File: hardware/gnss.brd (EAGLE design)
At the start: 33.5 x 34.6 mm, 39 parts, among them J1 MICRO_USB_B_HIROSE_ZX62-B-5PA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, SW1 TVAF06-A020B-R, U2 NJM12888F, X1 FA-238

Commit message: communication基盤一部改良、GNSS基盤
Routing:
- net GND: track 112.9 -> 180.1 mm, vias 71 -> 70
- net N$1: track 0.00 -> 35.7 mm, vias 0 -> 3
- net N$3: track 0.00 -> 22.1 mm, vias 0 -> 2
- net VDD: track 73.0 -> 91.8 mm, vias 6 -> 7
- net N$2: track 0.00 -> 3.50 mm

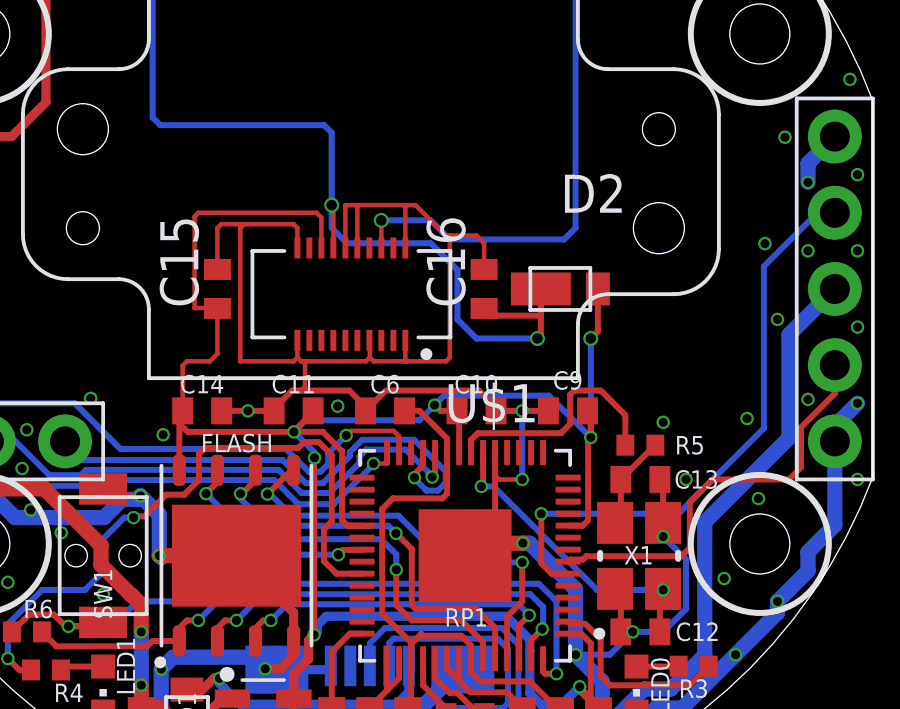
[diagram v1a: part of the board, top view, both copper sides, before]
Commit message: 変更点: communication_LoRaをUART接続に変換 gnss_GPSのRTX接続およびRESETの追加
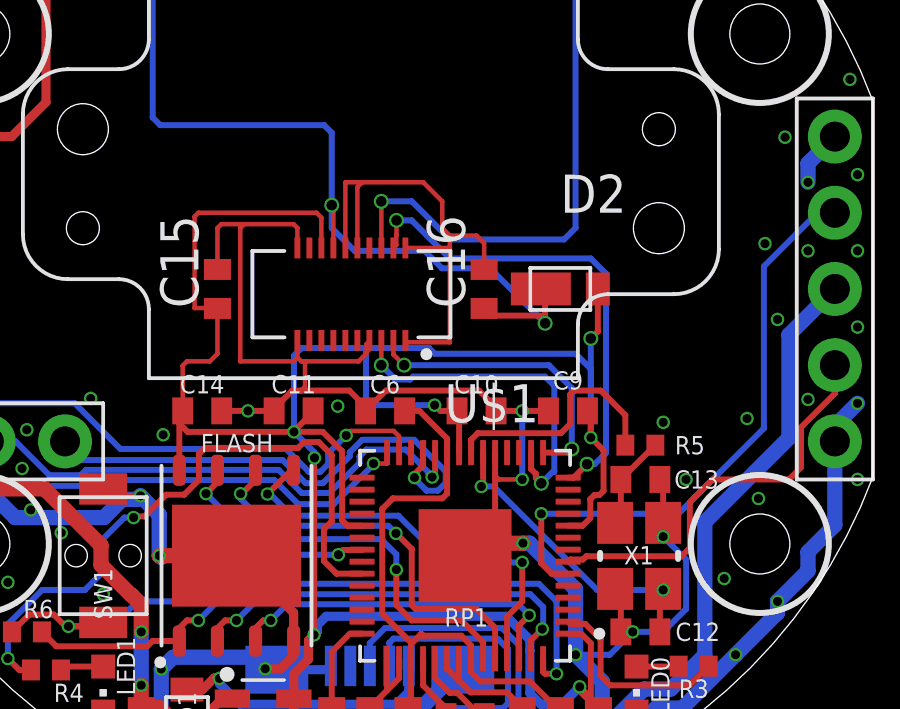
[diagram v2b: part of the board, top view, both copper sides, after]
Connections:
- removed net PWM5_A: RP1.13
- removed net PWM5_B: RP1.14
- removed net SPI1_CS: RP1.16
- removed net SPI1_MISO: RP1.15
- new net GPS_RESET: RP1.14, U$1.4
- new net GPS_RTX: RP1.16, U$1.5
- new net GPS_TRX: RP1.15, U$1.3
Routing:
- net GPS_RESET: track 0.00 -> 16.3 mm, vias 0 -> 2
- net GPS_RTX: track 0.00 -> 11.6 mm, vias 0 -> 2
- net GPS_TRX: track 0.00 -> 9.92 mm, vias 0 -> 2
- net VDD: track 91.8 -> 100.5 mm
- net N$1: track 35.7 -> 34.3 mm
- net N$3: track 22.1 -> 23.0 mm

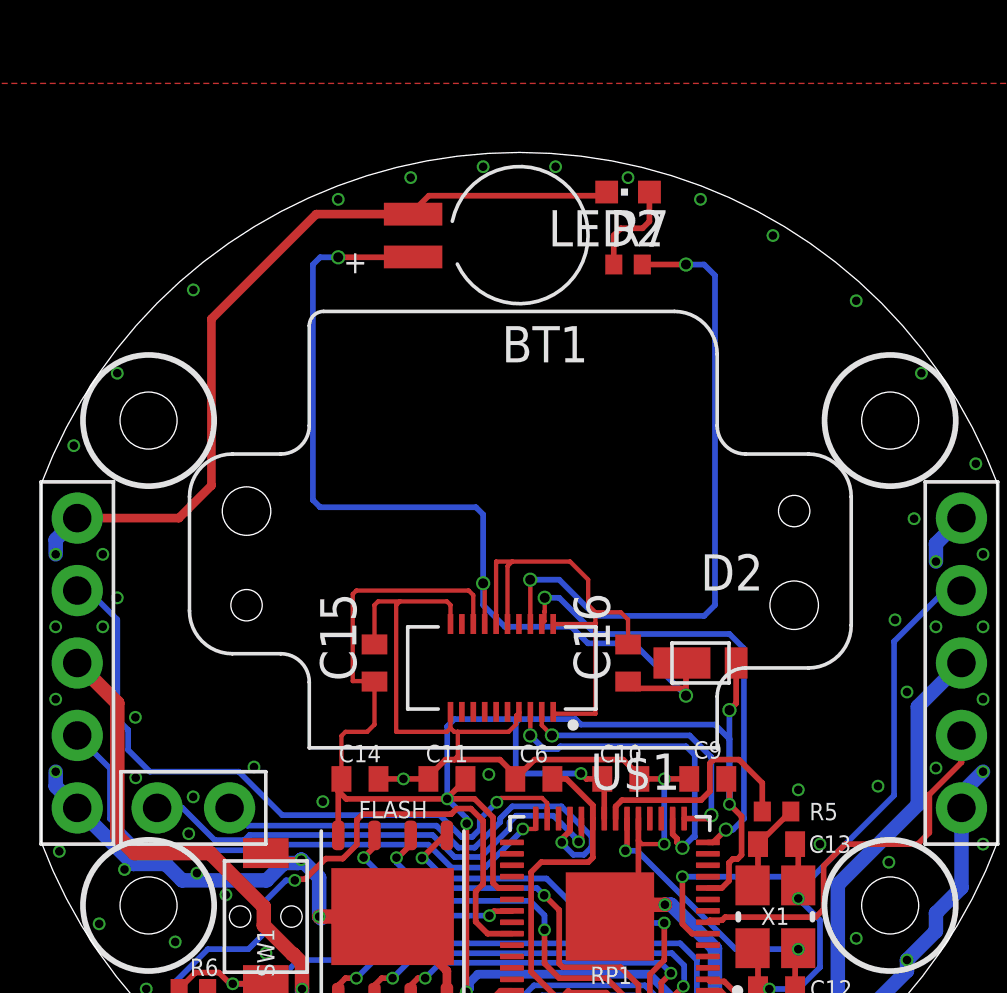
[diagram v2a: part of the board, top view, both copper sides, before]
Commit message: べたGND前です。esp32のschはノータッチなのでここに上がってないです。よろしくお願いします。
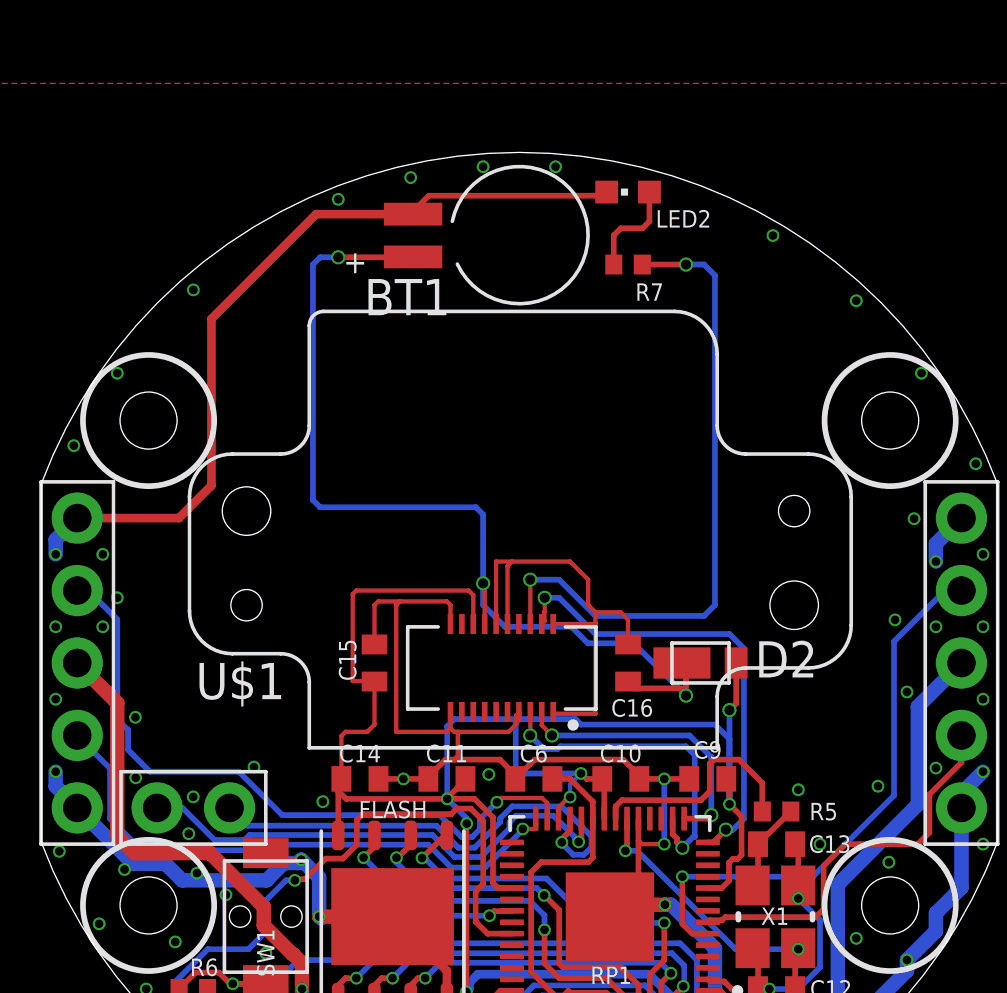
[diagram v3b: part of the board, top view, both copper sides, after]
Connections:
- net VDD: now also RP1.26
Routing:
- net VDD: track 100.5 -> 102.5 mm, vias 7 -> 8
- net GND: vias 70 -> 68
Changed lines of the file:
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@@
 <element name="BOTTOM" library="pins" package="P5_2.54" value="P5_2.54" x="15.5" y="0" smashed="yes"/>
 <element name="U$2" library="pins" package="P2_2.54" value="P2_2_2.54" x="-11.43" y="-5.08" smashed="yes" rot="R90">
-<attribute name="VALUE" x="-7.62" y="-7.62" size="0.8128" layer="27" font="vector" rot="R90"/>
+<attribute name="VALUE" x="-8.001" y="-2.667" size="0.8128" layer="27" font="vector" rot="R180"/>
 </element>
 <element name="U$1" library="gps" package="GYSFDMAXB" value="GYSFDMAXB" x="0.635" y="4.826" smashed="yes" rot="R180">
-<attribute name="NAME" x="5.635" y="-3.174" size="1.27" layer="25" rot="R180"/>
-<attribute name="VALUE" x="4.635" y="13.826" size="1.27" layer="27" rot="R180"/>
+<attribute name="NAME" x="-8.208" y="0.001" size="1.27" layer="25" rot="R180"/>
 </element>
 <element name="D2" library="diodes" package="CUHS20S30" value="CUHS20S30" x="6.35" y="0" smashed="yes">
-<attribute name="NAME" x="6.35" y="2.54" size="1.27" layer="25"/>
-<attribute name="VALUE" x="3.81" y="-2.54" size="1.27" layer="27"/>
+<attribute name="NAME" x="8.255" y="-0.508" size="1.27" layer="25"/>
 </element>
 <element name="LED2" library="led" library_urn="urn:adsk.eagle:library:259" package="CHIPLED_0603" package3d_urn="urn:adsk.eagle:package:15822/2" value="" x="3.81" y="16.51" smashed="yes" rot="R90">
-<attribute name="NAME" x="5.08" y="15.875" size="1.27" layer="25" rot="R180"/>
+<attribute name="NAME" x="6.731" y="15.875" size="0.6096" layer="25" font="vector" rot="R180"/>
 <attribute name="POPULARITY" value="28" x="-2.54" y="11.43" size="1.778" layer="27" rot="R90" display="off"/>
 <attribute name="VALUE" x="5.08" y="18.415" size="1.27" layer="27" rot="R180"/>
 </element>
 <element name="R7" library="rcl" library_urn="urn:adsk.eagle:library:334" package="R0402" package3d_urn="urn:adsk.eagle:package:23547/3" value="100" x="3.81" y="13.97" smashed="yes">
-<attribute name="NAME" x="3.175" y="14.605" size="1.27" layer="25"/>
+<attribute name="NAME" x="4.064" y="12.7" size="0.6096" layer="25" font="vector"/>
 <attribute name="POPULARITY" value="34" x="-1.27" y="20.32" size="1.778" layer="27" display="off"/>
 <attribute name="SPICEPREFIX" value="R" x="-1.27" y="20.32" size="1.778" layer="27" display="off"/>
-<attribute name="VALUE" x="3.175" y="12.065" size="1.27" layer="27"/>
 </element>
 <element name="C15" library="rcl" library_urn="urn:adsk.eagle:library:334" package="C0402" package3d_urn="urn:adsk.eagle:package:23626/2" value="0.1µ" x="-5.08" y="0" smashed="yes" rot="R90">
-<attribute name="NAME" x="-5.715" y="-0.635" size="1.27" layer="25" rot="R90"/>
+<attribute name="NAME" x="-5.715" y="-0.635" size="0.6096" layer="25" font="vector" rot="R90"/>
 <attribute name="POPULARITY" value="18" x="-5.08" y="0" size="1.778" layer="27" rot="R90" display="off"/>
 <attribute name="SPICEPREFIX" value="C" x="-5.08" y="0" size="1.778" layer="27" rot="R90" display="off"/>
-<attribute name="VALUE" x="-3.175" y="-0.635" size="1.27" layer="27" rot="R90"/>
 </element>
 <element name="C16" library="rcl" library_urn="urn:adsk.eagle:library:334" package="C0402" package3d_urn="urn:adsk.eagle:package:23626/2" value="0.1µ" x="3.81" y="0" smashed="yes" rot="R90">
-<attribute name="NAME" x="3.175" y="-0.635" size="1.27" layer="25" rot="R90"/>
+<attribute name="NAME" x="4.699" y="-1.27" size="0.6096" layer="25" font="vector" rot="R180"/>
 <attribute name="POPULARITY" value="18" x="3.81" y="0" size="1.778" layer="27" rot="R90" display="off"/>
 <attribute name="SPICEPREFIX" value="C" x="3.81" y="0" size="1.778" layer="27" rot="R90" display="off"/>
-<attribute name="VALUE" x="6.985" y="-0.254" size="1.27" layer="27" rot="R90"/>
 </element>
 <element name="BT1" library="MS414GE-FL26E" package="BAT_MS414GE-FL26E" value="MS414GE-FL26E" x="0" y="14.986" smashed="yes" rot="R180">
@@
 <attribute name="MF" value="Seiko" x="0" y="14.986" size="1.778" layer="27" rot="R180" display="off"/>
 <attribute name="MP" value="MS414GE-FL26E" x="0" y="14.986" size="1.778" layer="27" rot="R180" display="off"/>
-<attribute name="NAME" x="2.413" y="11.811" size="1.27" layer="25" rot="R180"/>
+<attribute name="NAME" x="-2.413" y="13.462" size="1.27" layer="25" rot="R180"/>
 <attribute name="PACKAGE" value="Custom Package Seiko" x="0" y="14.986" size="1.778" layer="27" rot="R180" display="off"/>
 <attribute name="PRICE" value="None" x="0" y="14.986" size="1.778" layer="27" rot="R180" display="off"/>
 <attribute name="PURCHASE-URL" value="https://pricing.snapeda.com/search/part/MS414GE-FL26E/?ref=eda" x="0" y="14.986" size="1.778" layer="27" rot="R180" display="off"/>
-<attribute name="VALUE" x="2.54" y="19.177" size="1.27" layer="27" rot="R180"/>
 </element>
 </elements>
@@
 <wire x1="7.79" y1="-5.377" x2="7.366" y2="-4.953" width="0.2" layer="1"/>
 <wire x1="7.096" y1="-7.89" x2="7.3495" y2="-7.6365" width="0.2" layer="1"/>
+<contactref element="RP1" pad="26"/>
+<via x="1.778" y="-4.7" extent="1-16" drill="0.3"/>
+<wire x1="1.605475" y1="-4.8318" x2="1.6462" y2="-4.8318" width="0.1524" layer="1"/>
+<wire x1="1.6462" y1="-4.8318" x2="1.778" y2="-4.7" width="0.1524" layer="1"/>
+<wire x1="1.375" y1="-5.455" x2="1.375" y2="-5.062275" width="0.1524" layer="1"/>
+<wire x1="1.375" y1="-5.062275" x2="1.605475" y2="-4.8318" width="0.1524" layer="1"/>
+<wire x1="2.159" y1="-3.873" x2="1.778" y2="-4.254" width="0.1524" layer="16"/>
+<wire x1="1.778" y1="-4.254" x2="1.778" y2="-4.7" width="0.1524" layer="16"/>
 </signal>
 <signal name="GND">
@@
 <via x="11.811" y="12.7" extent="1-16" drill="0.3"/>
 <via x="8.89" y="14.986" extent="1-16" drill="0.3"/>
-<via x="6.35" y="16.256" extent="1-16" drill="0.3"/>
-<via x="3.81" y="17.018" extent="1-16" drill="0.3"/>
 <via x="1.27" y="17.399" extent="1-16" drill="0.3"/>
 <via x="-1.27" y="17.399" extent="1-16" drill="0.3"/>
@@
 <wire x1="-14.605" y1="3.81" x2="-14.097" y2="2.286" width="0" layer="19" extent="1-1"/>
 <wire x1="-15.5" y1="5.08" x2="-14.605" y2="3.81" width="0" layer="19" extent="1-1"/>
-<wire x1="3.81" y1="17.018" x2="3.06" y2="16.51" width="0" layer="19" extent="1-1"/>
 <wire x1="-3.81" y1="17.018" x2="-3.725" y2="15.736" width="0" layer="19" extent="1-1"/>
 <wire x1="1.27" y1="17.399" x2="3.06" y2="16.51" width="0" layer="19" extent="1-1"/>
 <wire x1="-1.27" y1="17.399" x2="1.27" y2="17.399" width="0" layer="19" extent="1-1"/>
 <wire x1="-15.621" y1="7.62" x2="-15.5" y2="5.08" width="0" layer="19" extent="1-1"/>
-<wire x1="6.35" y1="16.256" x2="3.81" y2="17.018" width="0" layer="19" extent="1-1"/>
 <wire x1="-6.35" y1="16.256" x2="-3.81" y2="17.018" width="0" layer="19" extent="1-1"/>
-<wire x1="8.89" y1="14.986" x2="6.35" y2="16.256" width="0" layer="19" extent="1-1"/>
 <wire x1="-14.097" y1="10.16" x2="-15.621" y2="7.62" width="0" layer="19" extent="1-1"/>
+<wire x1="8.89" y1="14.986" x2="11.811" y2="12.7" width="0" layer="19" extent="1-1"/>
 <wire x1="-11.43" y1="13.081" x2="-14.097" y2="10.16" width="0" layer="19" extent="1-1"/>
 </signal>
@@
 <wire x1="2.575" y1="-6.823" x2="2.575" y2="-5.455" width="0.2" layer="1"/>
 <wire x1="0.4125" y1="-10.8265" x2="0.4125" y2="-7.3345" width="0.2" layer="1"/>
-<wire x1="1.158" y1="-4.064" x2="1.652" y2="-4.064" width="0.2" layer="1"/>
-<wire x1="2.575" y1="-4.987" x2="2.575" y2="-5.455" width="0.2" layer="1"/>
-<wire x1="1.652" y1="-4.064" x2="2.575" y2="-4.987" width="0.2" layer="1"/>
+<wire x1="1.158" y1="-4.064" x2="1.779" y2="-4.064" width="0.2" layer="1"/>
+<wire x1="2.575" y1="-4.86" x2="2.575" y2="-5.455" width="0.2" layer="1"/>
+<wire x1="1.779" y1="-4.064" x2="2.575" y2="-4.86" width="0.2" layer="1"/>
 </signal>
 <signal name="N$6">

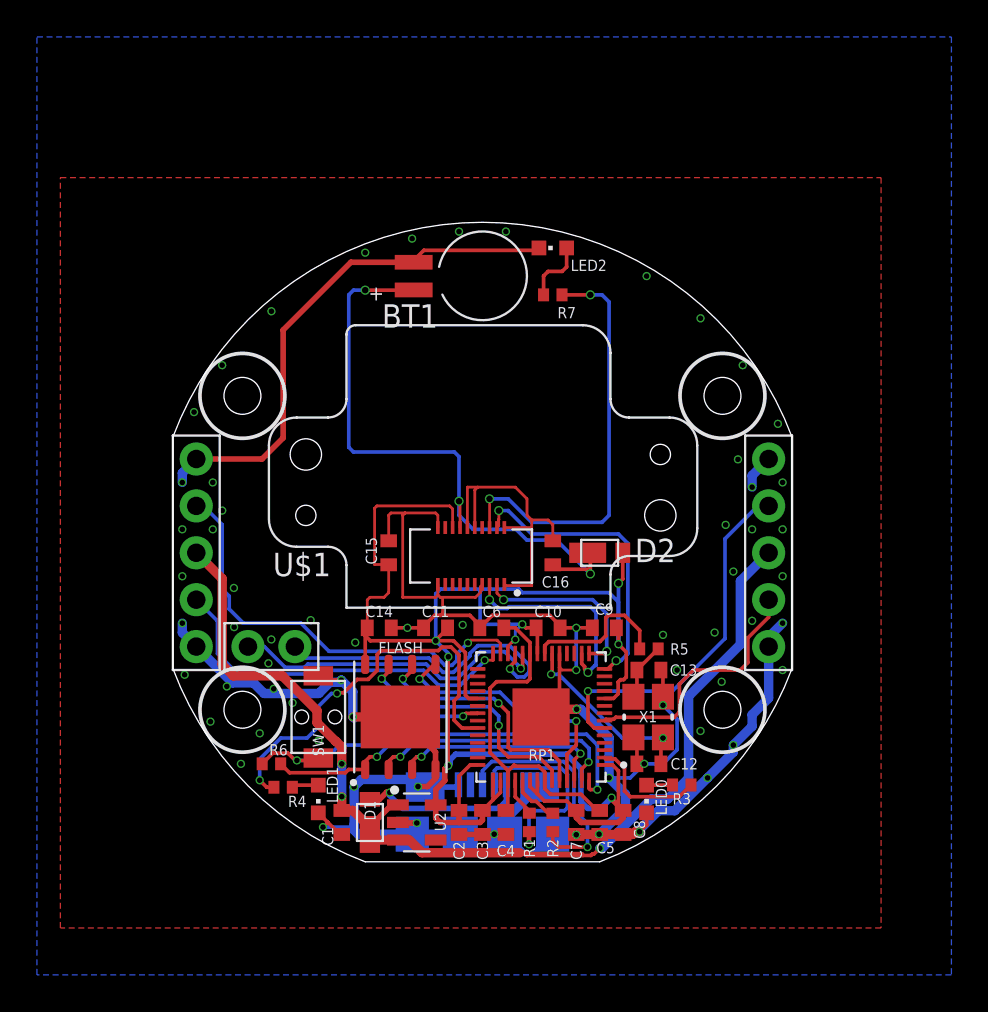
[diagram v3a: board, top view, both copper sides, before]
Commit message: LiPoのだけできなかったのですが、それ以外のべたGND済のものです。
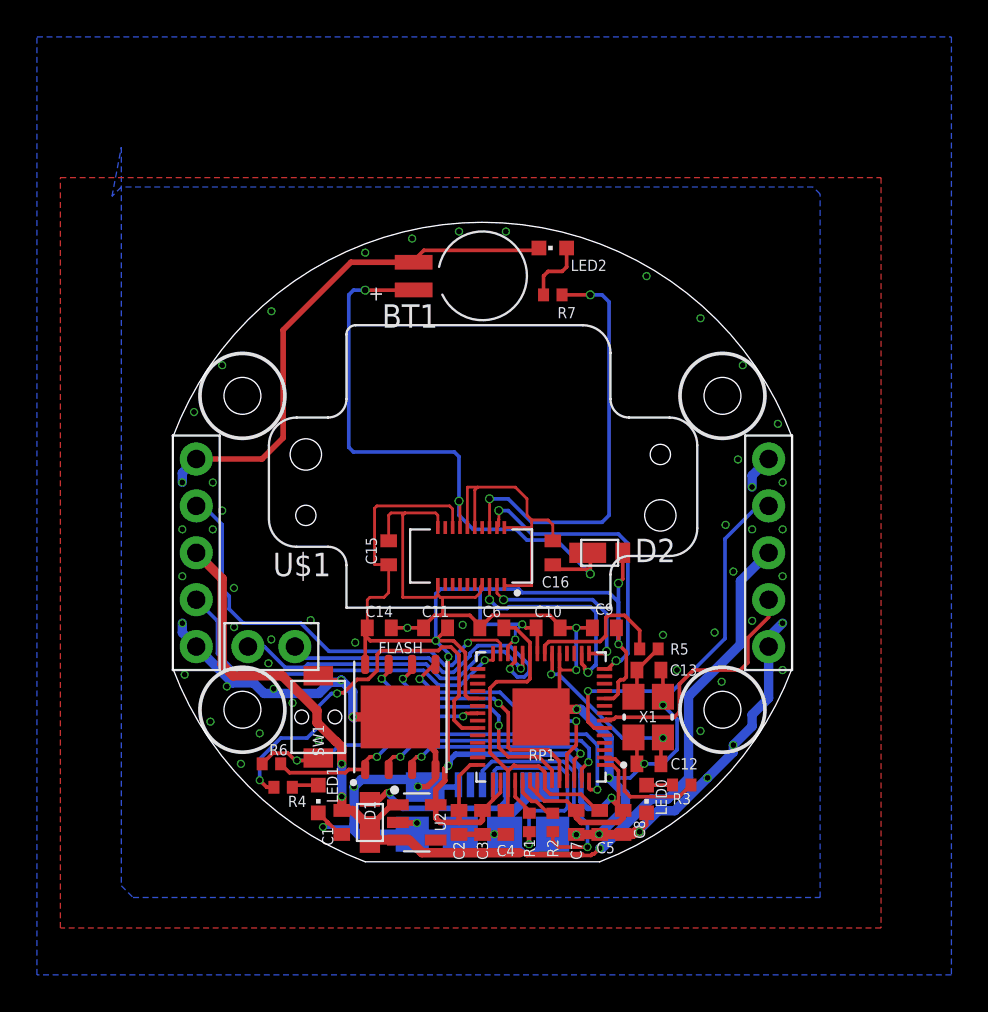
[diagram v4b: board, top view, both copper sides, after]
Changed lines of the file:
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@@
 <wire x1="-0.415" y1="3.395" x2="-0.254" y2="3.556" width="0.1524" layer="1"/>
 <wire x1="-0.415" y1="1.366" x2="-0.415" y2="3.395" width="0.1524" layer="1"/>
+<polygon width="0.1524" layer="16">
+<vertex x="-19.558" y="21.971"/>
+<vertex x="-19.558" y="-18.034"/>
+<vertex x="-18.923" y="-18.669"/>
+<vertex x="18.288" y="-18.669"/>
+<vertex x="18.288" y="19.431"/>
+<vertex x="17.907" y="19.812"/>
+<vertex x="-19.558" y="19.812"/>
+<vertex x="-20.066" y="19.304"/>
+</polygon>
 <wire x1="11.811" y1="12.7" x2="14.097" y2="10.16" width="0" layer="19" extent="1-1"/>
 <wire x1="16.002" y1="6.985" x2="14.097" y2="10.16" width="0" layer="19" extent="1-1"/>
